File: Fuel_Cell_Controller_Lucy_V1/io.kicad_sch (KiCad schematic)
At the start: 19 parts, among them J5 DA15_Receptacle_MountingHoles, J6 DE9_Receptacle, Q1 SI2302A-TPMSCT-ND, U6 MCP2542FD

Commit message: Making some layout changes, added solenoid controls with opto and bjt, changed MCU
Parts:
- removed D10, D9: SD0805S020S1R0, Diode_SMD:D_0805_2012Metric_Pad1.15x1.40mm_HandSolder, symbol Device:D_Schottky
- removed JP2, JP3: SolderJumper_2_Open, symbol Jumper:SolderJumper_2_Open
- removed Q1 (x2): SI2302A-TPMSCT-ND, Package_TO_SOT_SMD:SOT-23-3, symbol Device:Q_NMOS_GSD
- removed R8 (x2): 220, symbol Device:R_Small
- removed R8 (x2): 100k, symbol Device:R_Small
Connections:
- net CAN_H: now also R8.2
- net CAN_L: now also R8.2
- net CAN2_RX: no longer names the net of U6.4 (RXD)
- net CAN2_TX: no longer names the net of U6.1 (TXD)
- net CAN_STBY: no longer names the net of U6.8 (STBY)
- net PURGE_RETURN renamed PURGE_RTN
- net SUPPLY_RETURN renamed PURGE_VALVE
- net UNPROTECTED_12V renamed SUPPLY_RTN
- net SUPPLY_RTN: no longer J5.1
- net VDDA renamed MCU_REF
- new net SUPPLY_VALVE: J5.1
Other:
- added sheet Purge_Valve_Switch (12v_switch.kicad_sch)
- added sheet Supply_Valve_Switch (12v_switch.kicad_sch)
- note removed: "Should we add optocouplers? Select SMD diodes with high reverse volt prolly 50V High current tolerant NMOS as well. Check solenoid current req"
- note removed: "Solenoid Valve Controls"
- moved on the sheet: C28, J5, R8

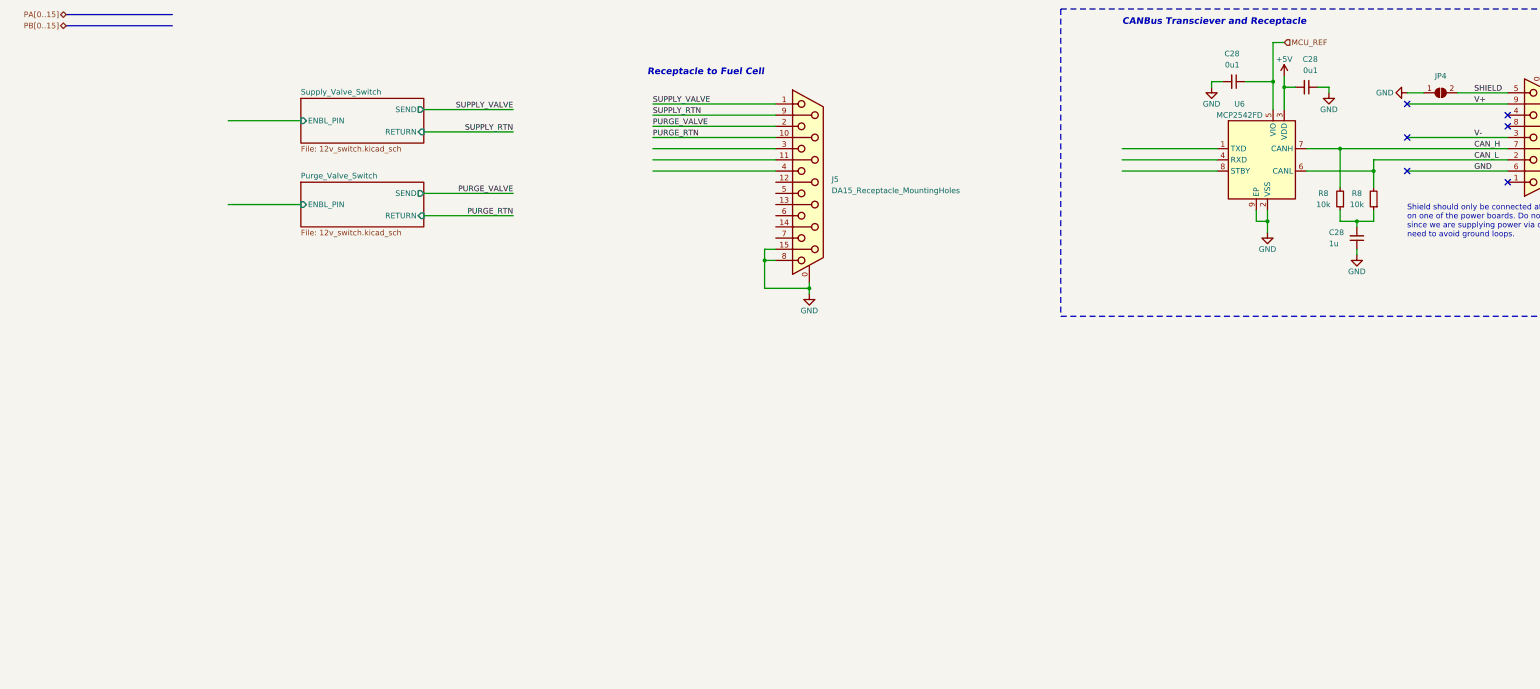
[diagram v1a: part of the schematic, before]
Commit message: started circuitry for the pressure sensor and thermistor on the fuel cell
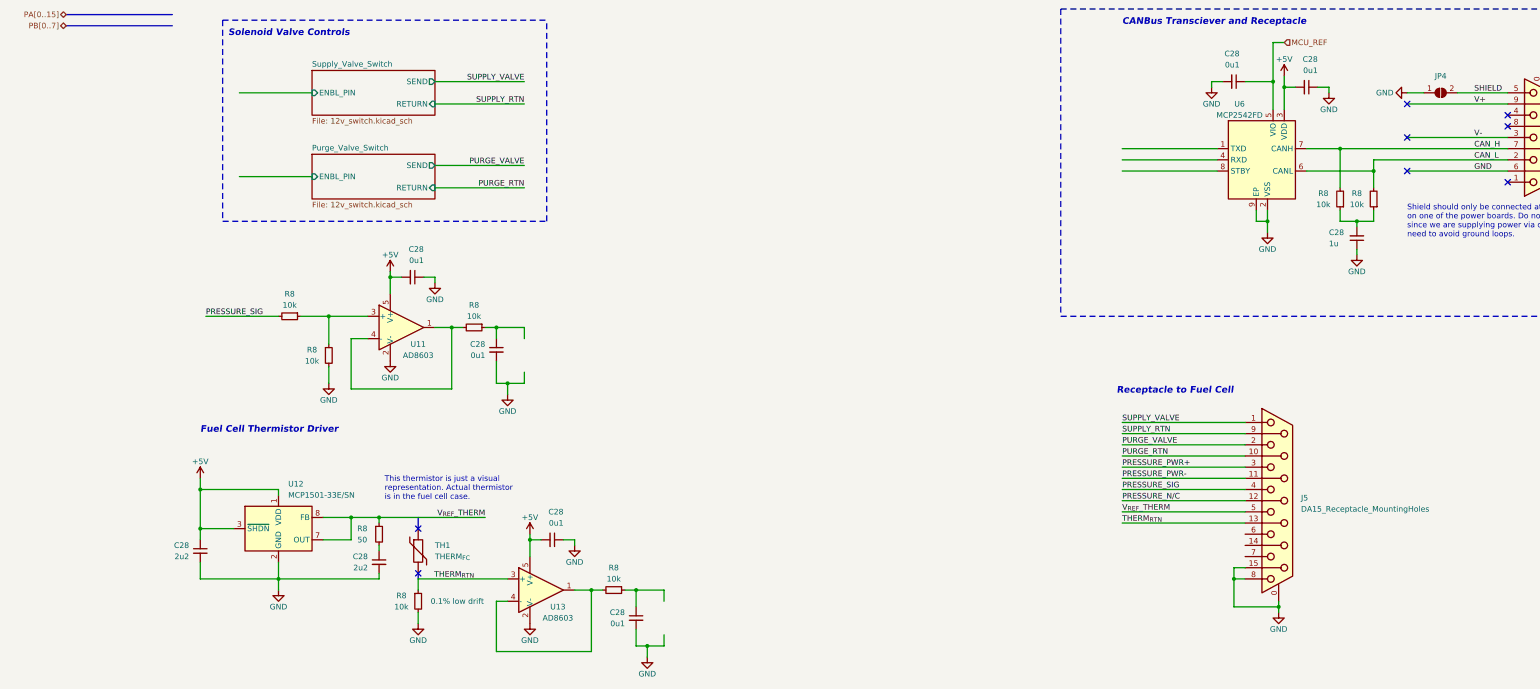
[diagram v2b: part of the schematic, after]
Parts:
- added C28 (x2): 2u2, symbol Device:C_Small
- added C28 (x4): 0u1, symbol Device:C_Small
- added R8 (x5): 10k, symbol Device:R_Small
- added R8: 50, symbol Device:R_Small
- added TH1: THERM_{FC}, symbol Device:Thermistor
- added U11, U13: AD8603, Package_TO_SOT_SMD:TSOT-23-5, symbol Amplifier_Operational:AD8603
- added U12: MCP1501-33E/SN, Package_SO:SOIC-8_3.9x4.9mm_P1.27mm, symbol Reference_Voltage:MCP1501-33xSN
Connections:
- net +5V: now also C28.1, C28.2, C28.2, U11.5 (V+), U12.1 (VDD), U12.3 (~{SHDN}), U13.5 (V+)
- net GND: now also C28.1, C28.1, C28.2, C28.2, C28.2, C28.2, R8.2, R8.2, U11.2 (V-), U12.2 (GND), U12.4 (GND), U12.5 (GND), U12.6 (GND), U13.2 (V-)
- net PRESSURE_PWR-: now reaches J5.11 (P111)
- net PRESSURE_N/C: now reaches J5.12 (P12)
- net THERM_{RTN}: now reaches J5.13 (P13)
- net THERM_{RTN}: now also R8.1, U13.3 (+)
- net PRESSURE_PWR+: now reaches J5.3
- net PRESSURE_SIG: now reaches J5.4
- net PRESSURE_SIG: now also R8.2
- net V_{REF}_THERM: now reaches J5.5
- net V_{REF}_THERM: now also R8.1, U12.7 (OUT), U12.8 (FB)
- new net: C28.1, R8.1 (x2)
- new net: R8.2, U11.1, U11.4 (-)
- new net: R8.1, R8.1, U11.3 (+)
- new net: C28.1, R8.2
- new net: R8.2, U13.1, U13.4 (-)
- no-connect marks 6 -> 8
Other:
- note added: "Fuel Cell Thermistor Driver"
- note added: "Solenoid Valve Controls"
- note added: "This thermistor is just a visual representation. Actual thermistor is in the fuel cell case."
- moved on the sheet: J5

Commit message: so much, can't explain
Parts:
- removed U6: MCP2542FD, Package_DFN_QFN:DFN-8-1EP_3x3mm_P0.65mm_EP1.55x2.4mm, symbol FCC_Parts:MCP2542FD
- added C20 (x3): 100n, Capacitor_SMD:C_0603_1608Metric, symbol Device:C_Small
- added C20 (x2): 47p, Capacitor_SMD:C_0603_1608Metric, symbol Device:C_Small
- added C20: 10n, Capacitor_SMD:C_0603_1608Metric, symbol Device:C_Small
- added C35: 4u7, symbol Device:C_Polarized_Small
- added D11 (x2): MMSZ5226B-7-F, FC.FTP:D_SOD_123_M, symbol FCC_Parts:MMSZ5226B-7-F
- added D4: LED, symbol Device:LED
- added J7: USB_B_Micro, RB_FTP:USB_Micro-B_Wuerth_629105150521, symbol Connector:USB_B_Micro
- added JP1: SolderJumper_2_Open, symbol Jumper:SolderJumper_2_Open
- added L1: 600R/0.5A, symbol Device:L_Iron
- added R28, R31: 27, symbol Device:R_Small
- added R32: 270, symbol Device:R_Small
- added U14: FT234XD-R, FC.FTP:SON45P300X300X80-13N, symbol FCC_Parts:FT234XD-R
- added U6: USBLC6-2SC6, FC.FTP:USBLC6-2SC6, symbol FCC_Parts:USBLC6-2SC6
- added U9: MCP2542FD-E/SN, Package_SO:SOIC-8_3.9x4.9mm_P1.27mm, symbol FCC_PARTS:MCP2542FD
- C28: value 1u -> 4u7
- C28: value 0u1 -> 100n
- R8: value 10k -> 60
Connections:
- net +5V: now also JP1.2 (B), U9.3 (VDD)
- net CAN_H: now also U9.7 (CANH)
- net CAN_L: now also U9.6 (CANL)
- net GND: now also C20.1, C20.2, C20.2, C20.2, C20.2, C20.2, C35.2, D11.2, D11.2, J7.5 (GND), J7.6 (Shield), U14.13 (GND__1), U14.5 (GND), U6.2, U9.2 (VSS)
- net at C28.1, R8.1: now also D11.1 (x2)
- net MCU_REF renamed +3V3
- net +3V3: now also U9.5 (VIO)
- net V_{REF}_THERM renamed THERM_{VREF}
- new net: C20.2, U14.2 (~{RESET}#)
- new net: C20.1, C35.1, JP1.1 (A), L1.1, U14.4 (VCC)
- new net: R28.1, U14.1 (USBDM)
- new net: R31.1, U14.12 (USBDP)
- new net: R32.2, U14.6 (CBUS0)
- new net: D4.1 (K), R32.1
- new net D+: J7.3 (D+), U6.4
- new net D-: J7.2 (D-), U6.6
- new net DM: C20.1, R28.2, U6.1
- new net DP: C20.1, R31.2, U6.3
- new net VCCIO: C20.1, D4.2 (A), U14.3 (3V3OUT), U14.9 (VCCIO)
- new net V_{BUS}: C20.1, J7.1 (VBUS), L1.2, U6.5
- no-connect marks 8 -> 9
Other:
- note added: "FC Pressure Sensor"
- note added: "FTDI - TTL to USB"
- note added: "FTDI VCP DRIVERS"
- note added: "Fuel Cell Thermistor"
- note added: "Run V_{BUS} under the IC close to GND pin for optimal protection"
- note added: "Solenoid Controls"
- note removed: "Fuel Cell Thermistor Driver"
- note removed: "Solenoid Valve Controls"
- moved on the sheet: C28, J5, R8, TH1, U11, U12, U13

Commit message: more things
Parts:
- removed R8: 10k, symbol Device:R_Small
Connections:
- net THERM_{RTN}: now also R8.2; no longer U13.3 (+)
- net PB1: now reaches C20.2, U14.2 (~{RESET}#)
- net at C28.1, R8.1: now also U13.3 (+); no longer D11.1
- net at C28.1: now also R8.1, R8.1, U11.3 (+); no longer D11.1
- net PA3: now reaches U11.1, U11.4 (-)
- net PA3: now also D11.1
- net PA9: now reaches U14.10 (RXD)
- net PB3: now reaches U14.11 (CTS#)
- net PA10: now reaches U14.7 (TXD)
- net PB4: now reaches U14.8 (RTS#)
- net PA4: now reaches U13.1, U13.4 (-)
- net PA4: now also D11.1; no longer R8.2
- net PA12: now reaches U9.1 (TXD)
- net PA11: now reaches U9.4 (RXD)
- net PA15: now reaches U9.8 (STBY)
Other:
- note added: "C_{1}"
- note added: "LPF must be before op-amp because input impedance of ADC is approx. 50k f_{c} ~= (R_{1}+R_{2})/(2*pi*R_{1}*R_{2}*C_{1})"
- note added: "R_{1}"
- note added: "R_{2}"
- moved on the sheet: C20, C28, C35, D11, D4, J7, JP1, L1, R28, R31, R32, R8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

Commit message: Again too much to say
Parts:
- C20: footprint Capacitor_SMD:C_0603_1608Metric -> Capacitor_SMD:C_0402_1005Metric
- C28: footprint (none) -> Capacitor_SMD:C_0603_1608Metric
- C28: value 100n -> 1u; footprint (none) -> Capacitor_SMD:C_0603_1608Metric
- C35: footprint (none) -> Capacitor_SMD:CP_Elec_3x5.3
- D4: footprint (none) -> LED_SMD:LED_0805_2012Metric
- J3: renamed from J6; footprint (none) -> Connector_Dsub:DSUB-9_Female_Horizontal_P2.77x2.84mm_EdgePinOffset7.70mm_Housed_MountingHolesOffset9.12mm
- J4: renamed from J5; footprint (none) -> Connector_Dsub:DSUB-15_Female_Horizontal_P2.77x2.84mm_EdgePinOffset7.70mm_Housed_MountingHolesOffset9.12mm
- JP1: footprint (none) -> Jumper:SolderJumper-2_P1.3mm_Open_RoundedPad1.0x1.5mm
- JP2: renamed from JP4; footprint (none) -> Jumper:SolderJumper-2_P1.3mm_Open_RoundedPad1.0x1.5mm
- L1: footprint (none) -> Inductor_SMD:L_0805_2012Metric
- R28, R31: footprint (none) -> Resistor_SMD:R_0402_1005Metric
- R32, R8: footprint (none) -> Resistor_SMD:R_0603_1608Metric
- renumbered U12 to U7, U11 to U8, U13 to U9
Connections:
- net PRESSURE_PWR+ is gone; now on net +5V: J4.3
- net PRESSURE_PWR- is gone; now on net GND: J4.11 (P111)
- net I2C_{SDA}: now reaches J4.14 (P14)
- net I2C_{SCL}: now reaches J4.6
- net PA3 renamed H2_{PRS}
- net PA4 renamed FC_{TEMP}
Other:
- note added: "Add I2C Add 5V for extern pressure"
- note added: "I_{Ref,max} = 20mA"
- note added: "R_{series} >= 3.3V/20mA = 165Ω"
- note added: "f_{c} = 15.9Hz"

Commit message: Most of the schematic done, pcb layout needs DRC
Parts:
- added C28: 3u, Capacitor_SMD:C_0805_2012Metric, symbol Device:C_Small
- added C28: 100n, Capacitor_SMD:C_0603_1608Metric, symbol Device:C_Small
- added D11: MMSZ5226B-7-F, FC.FTP:D_SOD_123_M, symbol FCC_Parts:MMSZ5226B-7-F
- added J6: Screw_Terminal_01x02, TerminalBlock_Phoenix:TerminalBlock_Phoenix_MKDS-1,5-2-5.08_1x02_P5.08mm_Horizontal, symbol Connector:Screw_Terminal_01x02
- added NT1: NetTie_2, NetTie:NetTie-2_SMD_Pad0.5mm, symbol Device:NetTie_2
- added R8: 1740, Resistor_SMD:R_0603_1608Metric, symbol Device:R_Small
- added R8: 660, Resistor_SMD:R_0603_1608Metric, symbol Device:R_Small
- added R8 (x2): 10k, Resistor_SMD:R_0603_1608Metric, symbol Device:R_Small
- added U17: AD8603, Package_TO_SOT_SMD:TSOT-23-5, symbol Amplifier_Operational:AD8603
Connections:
- net +5V: now also J4.7, C28.2, U17.5 (V+); no longer J4.3
- net GND: no longer C20.1, C20.2, C20.2, C20.2, C20.2, C20.2, C28.1, C28.1, C28.1, C28.1, C28.2, C28.2, C28.2, C28.2, C28.2, C35.2, D11.2, D11.2, J3.0 (PAD), J4.0 (PAD), J4.11 (P111), J4.15 (P15), J4.8, J7.5 (GND), J7.6 (Shield), JP2.1 (A), R8.2, R8.2, U14.13 (GND__1), U14.5 (GND), U6.2, U7.2 (GND), U7.4 (GND), U7.5 (GND), U7.6 (GND), U8.2 (V-), U9.2 (V-), U9.2 (VSS)
- new net: R8.1, R8.1, U17.3 (+)
- new net: C28.1, R8.2
- new net +12V: J4.3, R8.1
- new net BTN_{RTN}: J6.1 (Pin_1), R8.1, R8.2, R8.2
- new net GNDA: C20.1, C20.2, C20.2, C20.2, C20.2, C20.2, C28.1, C28.1, C28.1, C28.1, C28.1, C28.2, C28.2, C28.2, C28.2, C28.2, C28.2, C35.2, D11.2, D11.2, D11.2, J3.0 (PAD), J4.0 (PAD), J4.11 (P111), J4.15 (P15), J4.8, J6.2 (Pin_2), J7.6 (Shield), JP2.1 (A), NT1.1, R8.2, R8.2, R8.2, U14.13 (GND__1), U14.5 (GND), U17.2 (V-), U7.2 (GND), U7.4 (GND), U7.5 (GND), U7.6 (GND), U8.2 (V-), U9.2 (V-), U9.2 (VSS)
- new net GND_{1}: J7.5 (GND), NT1.2, U6.2
- new net PA3: D11.1, U17.1, U17.4 (-)
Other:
- note added: "De-bounce circuitry with external button represented by the terminal"
- note added: "Driver Start/Stop"
- note added: "Ext SPST Button"
- note added: "Volt/Div Buffer to bring 12V down to 3.3V"
- note removed: "Add I2C Add 5V for extern pressure"

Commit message: $
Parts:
- C20: value 10n -> 100n
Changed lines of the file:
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@@
       (effects (font (size 1.27 1.27)) (justify left))
     )
-    (property "Value" "10n" (at 381 201.93 0)
+    (property "Value" "100n" (at 382.27 201.93 0)
       (effects (font (size 1.27 1.27)) (justify right))
     )

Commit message: things
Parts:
- R8: value 10k -> 100k
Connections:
- net GNDA: now also J4.13 (P13), TH1.2; no longer R8.2
- net THERM_{VREF}: now also R8.2, R8.2, TH1.1; no longer R8.1, U7.7 (OUT), U7.8 (FB)
- removed net THERM_{RTN}: J4.13 (P13), R8.1, R8.2
- new net: R8.1, R8.1, U7.7 (OUT), U7.8 (FB)
- no-connect marks 9 -> 7
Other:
- note added: "The resistance of TH1 @ 25°C is 100k To linearize about 25°C R23 = ${72cd9925-16f5-4224-9154-4bbf866d9118:VALUE} low side"
- moved on the sheet: R8, TH1
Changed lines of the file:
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@@
   (junction (at 246.38 63.5) (diameter 0) (color 0 0 0 0)
   )
+  (junction (at 69.85 156.21) (diameter 0) (color 0 0 0 0)
+  )
   (junction (at 228.6 54.61) (diameter 0) (color 0 0 0 0)
   )
@@
   (junction (at 297.18 210.82) (diameter 0) (color 0 0 0 0)
   )
+  (junction (at 69.85 171.45) (diameter 0) (color 0 0 0 0)
+  )
   (junction (at 302.26 31.75) (diameter 0) (color 0 0 0 0)
   )
@@
   )
   (no_connect (at 353.06 53.34))
-  (no_connect (at 69.85 154.94))
   (no_connect (at 330.2 43.18))
-  (no_connect (at 69.85 144.78))
   (no_connect (at 389.89 205.74))
   (no_connect (at 330.2 35.56))
@@
     (stroke (width 0) (type default))
   )
-  (wire (pts (xy 60.96 142.24) (xy 85.09 142.24))
+  (wire (pts (xy 60.96 142.24) (xy 69.85 142.24))
     (stroke (width 0) (type default))
   )
@@
     (stroke (width 0) (type default))
   )
-  (polyline (pts (xy 69.85 142.24) (xy 69.85 144.78))
-    (stroke (width 0) (type default))
-  )
   (wire (pts (xy 328.93 114.3) (xy 356.87 114.3))
     (stroke (width 0) (type default))
@@
     (stroke (width 0) (type default))
   )
+  (wire (pts (xy 69.85 142.24) (xy 69.85 147.32))
+    (stroke (width 0) (type default))
+  )
   (wire (pts (xy 311.15 200.66) (xy 313.69 200.66))
     (stroke (width 0) (type default))
@@
     (stroke (width 0) (type default))
   )
+  (wire (pts (xy 69.85 152.4) (xy 69.85 156.21))
+    (stroke (width 0) (type default))
+  )
   (wire (pts (xy 389.89 203.2) (xy 387.35 203.2))
     (stroke (width 0) (type default))
@@
     (stroke (width 0.8) (type dash))
   )
-  (polyline (pts (xy 69.85 154.94) (xy 69.85 156.21))
-    (stroke (width 0) (type default))
-  )
   (wire (pts (xy 68.58 80.01) (xy 68.58 81.28))
     (stroke (width 0) (type default))
@@
     (stroke (width 0.8) (type dash))
   )
-  (wire (pts (xy 69.85 163.83) (xy 69.85 166.37))
+  (wire (pts (xy 69.85 171.45) (xy 69.85 173.99))
     (stroke (width 0) (type default))
   )
@@
     (stroke (width 0) (type default))
   )
+  (wire (pts (xy 69.85 171.45) (xy 82.55 171.45))
+    (stroke (width 0) (type default))
+  )
   (polyline (pts (xy 13.97 67.31) (xy 87.63 67.31))
     (stroke (width 0.8) (type dash))
@@
     (stroke (width 0) (type default))
   )
+  (wire (pts (xy 69.85 168.91) (xy 69.85 171.45))
+    (stroke (width 0) (type default))
+  )
   (wire (pts (xy 314.96 59.69) (xy 314.96 62.23))
     (stroke (width 0) (type default))
@@
   )
   (text "This thermistor is just a visual\nrepresentation. Actual thermistor\nis in the fuel cell case."
-    (at 62.23 138.43 0)
+    (at 60.96 134.62 0)
     (effects (font (size 1.27 1.27)) (justify left bottom))
   )
@@
     (effects (font (size 1.27 1.27)) (justify left bottom))
   )
+  (text "The resistance of TH1 @ 25°C is 100k\nTo linearize about 25°C\nR23 = ${72cd9925-16f5-4224-9154-4bbf866d9118:VALUE} low side"
+    (at 77.47 180.34 0)
+    (effects (font (size 1.27 1.27)) (justify left bottom))
+  )
   (text "FTDI - TTL to USB" (at 245.11 163.83 0)
     (effects (font (size 2.5 2.5) (thickness 0.5) bold italic) (justify left bottom))
@@
     (effects (font (size 1.27 1.27)) (justify left bottom))
   )
-  (text "R_{series} >= 3.3V/20mA = 165Ω" (at 54.61 176.53 0)
+  (text "R_{series} >= 3.3V/20mA = 165Ω" (at 21.59 168.91 0)
     (effects (font (size 1.27 1.27)) (justify left bottom))
   )
@@
     (effects (font (size 1.27 1.27)) (justify left bottom))
   )
-  (label "THERM_{RTN}" (at 85.09 156.21 180) (fields_autoplaced)
+  (label "THERM_{RTN}" (at 82.55 171.45 180) (fields_autoplaced)
     (effects (font (size 1.27 1.27)) (justify right bottom))
   )
@@
     (effects (font (size 1.27 1.27)) (justify right bottom))
   )
-  (label "THERM_{VREF}" (at 85.09 142.24 180) (fields_autoplaced)
+  (label "THERM_{VREF}" (at 82.55 156.21 180) (fields_autoplaced)
     (effects (font (size 1.27 1.27)) (justify right bottom))
   )
@@
     )
   )
-  (symbol (lib_id "Device:R_Small") (at 69.85 161.29 0) (unit 1)
+  (symbol (lib_id "Device:R_Small") (at 69.85 149.86 0) (mirror y) (unit 1)
     (in_bom yes) (on_board yes) (dnp no)
-    (property "Reference" "R8" (at 66.04 160.02 0)
+    (property "Reference" "R8" (at 73.66 148.59 0)
       (effects (font (size 1.27 1.27)))
     )
-    (property "Value" "10k" (at 66.04 162.56 0)
+    (property "Value" "100k" (at 73.66 151.13 0)
       (effects (font (size 1.27 1.27)))
     )
-    (property "Footprint" "Resistor_SMD:R_0603_1608Metric" (at 69.85 161.29 0)
+    (property "Footprint" "Resistor_SMD:R_0603_1608Metric" (at 69.85 149.86 0)
       (effects (font (size 1.27 1.27)) hide)
     )
-    (property "Datasheet" "~" (at 69.85 161.29 0)
+    (property "Datasheet" "~" (at 69.85 149.86 0)
       (effects (font (size 1.27 1.27)) hide)
     )
-    (property "Desc" "0.1% low drift" (at 78.74 161.29 0)
+    (property "Desc" "0.1% low drift" (at 78.74 146.05 0)
       (effects (font (size 1.27 1.27)))
     )
@@
     )
   )
-  (symbol (lib_id "power:GNDA") (at 69.85 166.37 0) (mirror y) (unit 1)
+  (symbol (lib_id "power:GNDA") (at 69.85 173.99 0) (mirror y) (unit 1)
     (in_bom yes) (on_board yes) (dnp no)
-    (property "Reference" "#PWR023" (at 69.85 172.72 0)
+    (property "Reference" "#PWR023" (at 69.85 180.34 0)
       (effects (font (size 1.27 1.27)) hide)
     )
-    (property "Value" "GNDA" (at 67.31 171.45 0)
+    (property "Value" "GNDA" (at 67.31 179.07 0)
       (effects (font (size 1.27 1.27)) (justify right))
     )
-    (property "Footprint" "" (at 69.85 166.37 0)
+    (property "Footprint" "" (at 69.85 173.99 0)
       (effects (font (size 1.27 1.27)) hide)
     )
-    (property "Datasheet" "" (at 69.85 166.37 0)
+    (property "Datasheet" "" (at 69.85 173.99 0)
       (effects (font (size 1.27 1.27)) hide)
     )
@@
     )
   )
-  (symbol (lib_id "Device:Thermistor") (at 69.85 149.86 0) (unit 1)
+  (symbol (lib_id "Device:Thermistor") (at 69.85 163.83 0) (unit 1)
     (in_bom no) (on_board no) (dnp no) (fields_autoplaced)
-    (property "Reference" "TH1" (at 73.66 148.59 0)
+    (property "Reference" "TH1" (at 73.66 162.56 0)
       (effects (font (size 1.27 1.27)) (justify left))
     )
-    (property "Value" "THERM_{FC}" (at 73.66 151.13 0)
+    (property "Value" "THERM_{FC}" (at 73.66 165.1 0)
       (effects (font (size 1.27 1.27)) (justify left))
     )
-    (property "Footprint" "" (at 69.85 149.86 0)
+    (property "Footprint" "" (at 69.85 163.83 0)
       (effects (font (size 1.27 1.27)) hide)
     )
-    (property "Datasheet" "~" (at 69.85 149.86 0)
+    (property "Datasheet" "~" (at 69.85 163.83 0)
       (effects (font (size 1.27 1.27)) hide)
     )
